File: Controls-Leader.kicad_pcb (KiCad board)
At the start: 2 copper layers, 79.2 x 97.5 mm, 188 parts, among them J1 ExtraADCs, J10 A_PRCHG_BYPASS, J11 M_PRCHG_BYPASS, J12 Brake_Sw, J13 UART_TP, J14 CAN_DB9, J15 Conn_02x03_Odd_Even, J16 M_CAN_DB9, J17 M_CNTCTR, J18 PowerConn, J2 UART_TP, J21 CAN_IN, J22 CAN_OUT, J23 USB_B_Micro, J25 UART_TP, J27 CAN_TP, J3 ExtraGPIO_Conn, J4 Dashboard, J5 M_CAN_IN, J6 Display, J7 Accel_Pot, J8 SWD, J9 Brake_Pot, Q1 IRLML0030, Q2 IRLML0030, Q3 IRLML0030, Q4 IRLML0030, Q5 IRLML0030, Q6 IRLML0030, SW10 RESET, U1 EL3H7, U10 EL3H7, U12 RI3-1205S, U13 NCP1117-3.3_SOT223, U14 ADM3055E, U15 CDSOT23-T24CAN, U17 ADM3055E, U18 CDSOT23-T24CAN, U19 CP2102N-A01-GQFN24, U2 EL3H7, U23 EL3H7, U24 EL3H7, U25 EL3H7, U26 EL3H7, U27 EL3H7, U28 EL3H7, U29 EL3H7, U3 EL3H7, U4 EL3H7, U5 EL3H7, U6 EL3H7, U7 STM32F413RHTx, U8 EL3H7, U9 EL3H7, Y1 Crystal

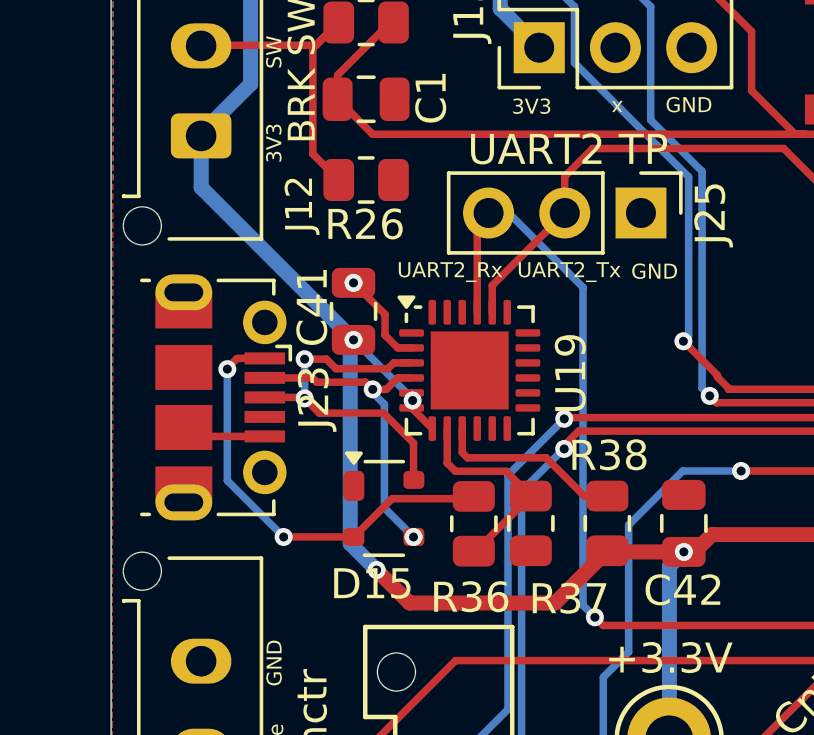
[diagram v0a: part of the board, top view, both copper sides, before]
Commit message: Removed vias in small pads.
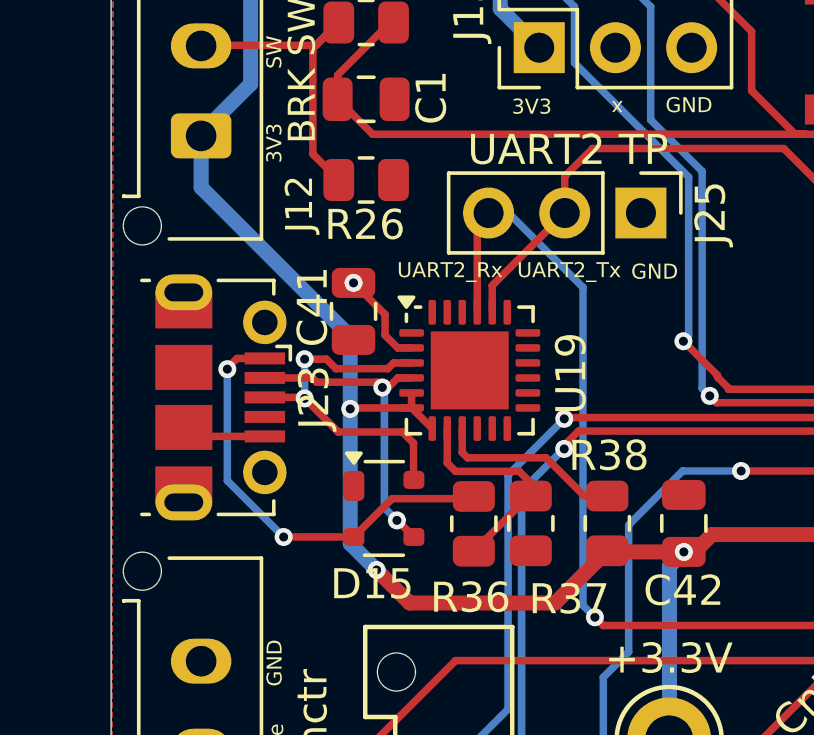
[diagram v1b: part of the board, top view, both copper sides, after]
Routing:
- net +3.3V: track 315.9 -> 315.1 mm, vias 25 -> 24

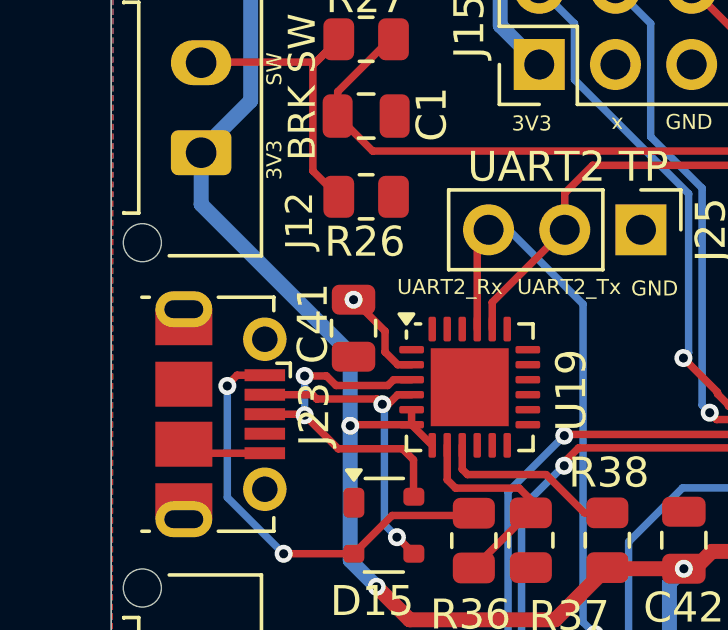
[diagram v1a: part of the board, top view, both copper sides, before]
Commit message: Added common libraries as a submodule, updated gitignore and library paths, reconnected item (my bad, sorry about that).
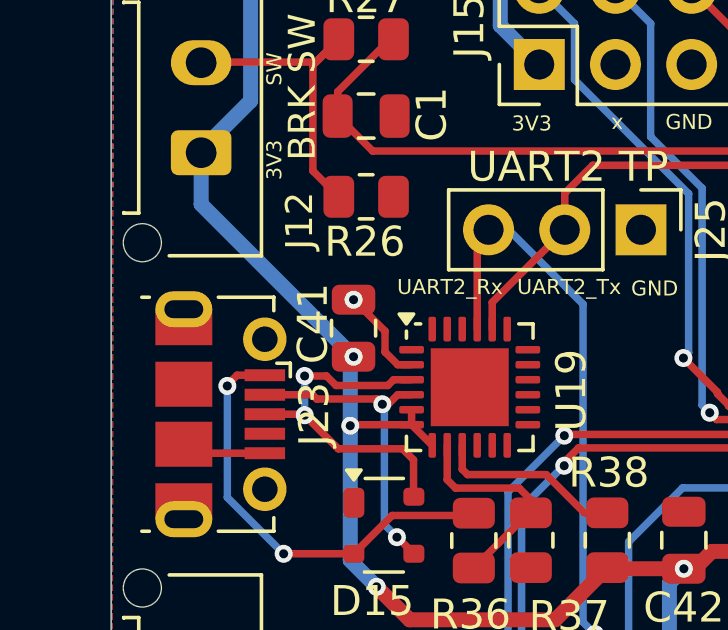
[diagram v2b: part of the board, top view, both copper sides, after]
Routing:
- net +3.3V: track 315.1 -> 315.2 mm, vias 24 -> 25
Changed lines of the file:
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@@
+	)
+	(via
+		(at 120.58 100.579998)
+		(size 0.6)
+		(drill 0.3)
+		(layers "F.Cu" "B.Cu")
+		(net 5)
 	)
 	(via
@@
 	)
 	(segment
+		(start 115.5 95.499998)
+		(end 115.5 93.78)
+		(width 0.5)
+		(layer "B.Cu")
+		(net 5)
+	)
+	(segment
+		(start 120.58 100.579998)
+		(end 115.5 95.499998)
+		(width 0.5)
+		(layer "B.Cu")
+		(net 5)
+	)
+	(segment
 		(start 167.85398 96.226046)
 		(end 167.85398 90.02398)
@@
 	)
 	(segment
-		(start 120.47 102.88)
-		(end 120.47 100.469998)
-		(width 0.5)
-		(layer "B.Cu")
-		(net 5)
-	)
-	(segment
 		(start 131.2 121.4)
 		(end 131.2 119.51)
@@
 	)
 	(segment
-		(start 120.47 100.469998)
-		(end 115.5 95.499998)
-		(width 0.5)
-		(layer "B.Cu")
-		(net 5)
-	)
-	(segment
 		(start 121.0875 80.215999)
 		(end 121.0875 74.7125)
@@
 	)
 	(segment
+		(start 120.47 102.88)
+		(end 120.47 100.689998)
+		(width 0.5)
+		(layer "B.Cu")
+		(net 5)
+	)
+	(segment
 		(start 117.15 84.26)
 		(end 117.15 92.05)
@@
 	)
 	(segment
-		(start 115.5 95.499998)
-		(end 115.5 93.78)
-		(width 0.5)
-		(layer "B.Cu")
-		(net 5)
-	)
-	(segment
 		(start 158.2 105.25)
 		(end 157.7 104.75)
@@
 		(width 0.5)
 		(layer "B.Cu")
+		(net 5)
+	)
+	(segment
+		(start 120.47 100.689998)
+		(end 120.58 100.579998)
+		(width 0.5)
+		(layer "B.Cu")

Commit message: DRC errors gone whoa
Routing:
- net GND: track 19.5 -> 18.2 mm
- net /NRST: track 21.4 -> 22.1 mm
- net /IG1: track 25.5 -> 26.1 mm
